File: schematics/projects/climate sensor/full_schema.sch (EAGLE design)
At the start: 35 parts, among them Q1 KT3102BM, Q2 KT3102BM, Q3 KT3102BM, Q4 KT3102BM, Q5 KT3102BM

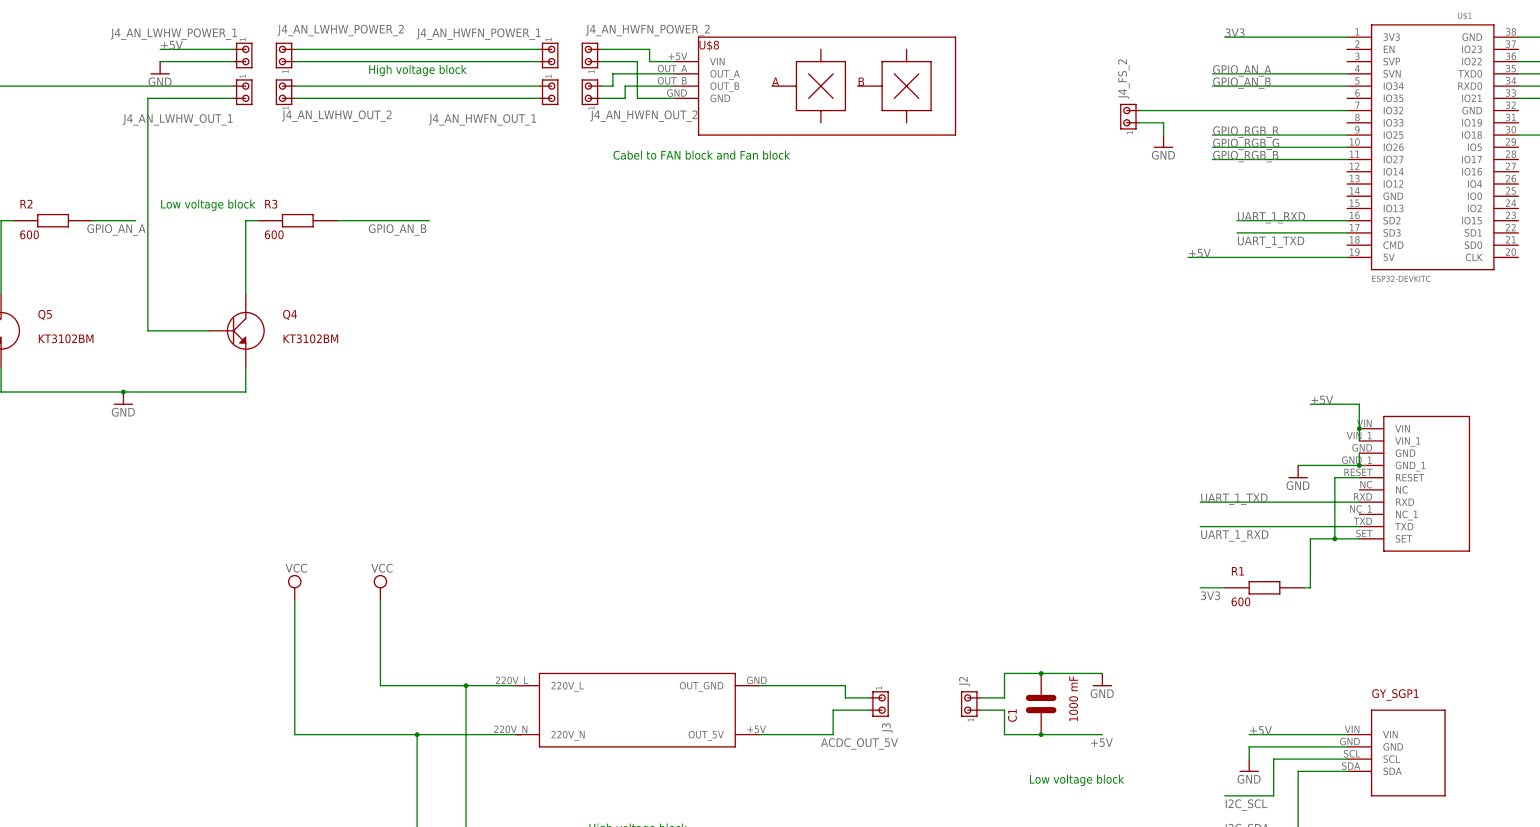
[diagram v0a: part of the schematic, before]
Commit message: added eagle board files for low-voltage schemas
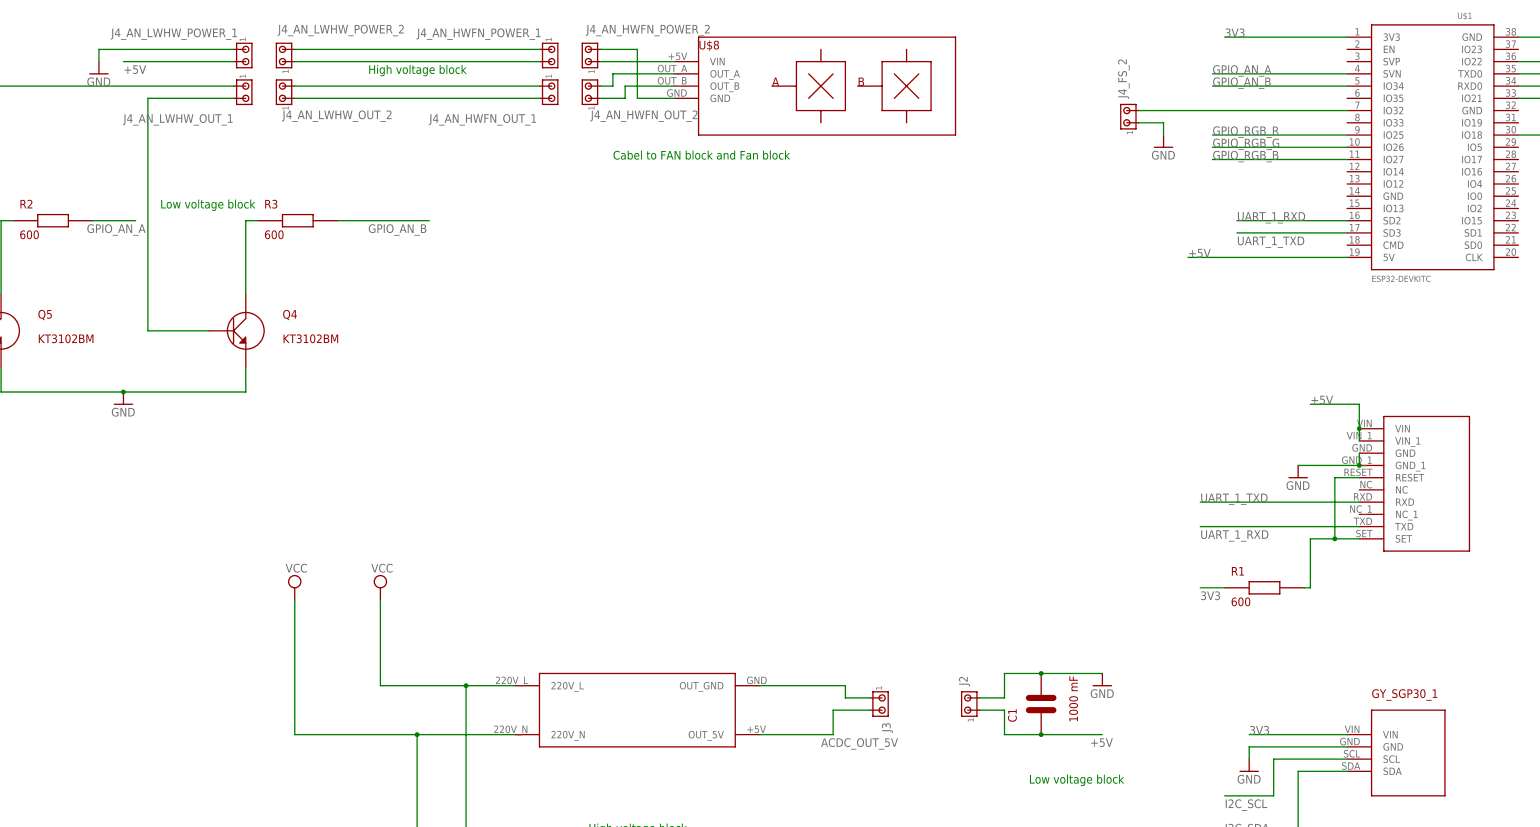
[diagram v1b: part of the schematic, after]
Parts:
- renumbered GY_SGP1 to GY_SGP30_1
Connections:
- net +5V: now also J4_AN_LWHW_POWER_1.2; no longer GY_SGP30_1.VIN, J4_AN_LWHW_POWER_1.1
- net 3V3: now also GY_SGP30_1.VIN
- net GND: now also J4_AN_HWFN_POWER_2.2, J4_AN_LWHW_POWER_1.1; no longer J4_AN_HWFN_POWER_2.1, J4_AN_LWHW_POWER_1.2
- net N$12: now also J4_AN_HWFN_POWER_2.1; no longer J4_AN_HWFN_POWER_2.2
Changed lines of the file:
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@@
 <part name="U$10" library="my_devices" deviceset="FAN" device=""/>
 <part name="U$3" library="my_devices" deviceset="PMS7003" device=""/>
-<part name="GY_SGP1" library="my_devices" deviceset="GY-SGP30" device=""/>
+<part name="GY_SGP30_1" library="my_devices" deviceset="GY-SGP30" device=""/>
 <part name="U$5" library="my_devices" deviceset="TTP223" device=""/>
 <part name="U$6" library="my_devices" deviceset="RGBLED" device=""/>
@@
 <part name="J4_AN_HWFN_POWER_2" library="con-amp" library_urn="urn:adsk.eagle:library:127" deviceset="MTA02-100" device="" package3d_urn="urn:adsk.eagle:package:8081649/1"/>
 <part name="J4_AN_HWFN_OUT_2" library="con-amp" library_urn="urn:adsk.eagle:library:127" deviceset="MTA02-100" device="" package3d_urn="urn:adsk.eagle:package:8081649/1"/>
-<part name="GND10" library="supply1" library_urn="urn:adsk.eagle:library:371" deviceset="GND" device=""/>
 <part name="J8" library="con-amp" library_urn="urn:adsk.eagle:library:127" deviceset="MTA02-100" device="" package3d_urn="urn:adsk.eagle:package:8081649/1"/>
 <part name="J9" library="con-amp" library_urn="urn:adsk.eagle:library:127" deviceset="MTA02-100" device="" package3d_urn="urn:adsk.eagle:package:8081649/1"/>
@@
 <part name="J4_AN_HWFN_OUT_1" library="con-amp" library_urn="urn:adsk.eagle:library:127" deviceset="MTA02-100" device="" package3d_urn="urn:adsk.eagle:package:8081649/1"/>
 <part name="J4_AN_HWFN_POWER_1" library="con-amp" library_urn="urn:adsk.eagle:library:127" deviceset="MTA02-100" device="" package3d_urn="urn:adsk.eagle:package:8081649/1"/>
+<part name="GND3" library="supply1" library_urn="urn:adsk.eagle:library:371" deviceset="GND" device=""/>
 </parts>
 <sheets>
@@
 <instance part="U$10" gate="G$1" x="-93.98" y="-106.68" smashed="yes" rot="R90" grouprefs="FAN"/>
 <instance part="U$3" gate="G$1" x="-38.1" y="10.16" smashed="yes" grouprefs="PMS7003"/>
-<instance part="GY_SGP1" gate="G$1" x="-48.26" y="-43.18" smashed="yes" grouprefs="GY-SGP30">
+<instance part="GY_SGP30_1" gate="G$1" x="-48.26" y="-43.18" smashed="yes" grouprefs="GY-SGP30">
 <attribute name="NAME" x="-50.8" y="-33.02" size="1.778" layer="94"/>
 </instance>
@@
 <attribute name="VALUE" x="-209.55" y="96.52" size="1.778" layer="96" rot="R90"/>
 </instance>
-<instance part="GND10" gate="1" x="-302.26" y="96.52" smashed="yes" grouprefs="ANEMOMETER">
-<attribute name="VALUE" x="-304.8" y="93.98" size="1.778" layer="96"/>
-</instance>
 <instance part="J8" gate="G$1" x="-149.86" y="-109.22" smashed="yes" rot="R270" grouprefs="FAN_SWITCH">
 <attribute name="NAME" x="-149.86" y="-114.3" size="1.778" layer="95" rot="R270"/>
@@
 <attribute name="NAME" x="-248.92" y="104.14" size="1.778" layer="95"/>
 <attribute name="VALUE" x="-224.79" y="96.52" size="1.778" layer="96" rot="R270"/>
+</instance>
+<instance part="GND3" gate="1" x="-314.96" y="96.52" smashed="yes" grouprefs="ANEMOMETER">
+<attribute name="VALUE" x="-317.5" y="93.98" size="1.778" layer="96"/>
 </instance>
 </instances>
@@
 <pinref part="GND6" gate="1" pin="GND"/>
 <wire x1="-76.2" y1="-43.18" x2="-76.2" y2="-45.72" width="0.1524" layer="91" grouprefs="GY-SGP30"/>
-<pinref part="GY_SGP1" gate="G$1" pin="GND"/>
+<pinref part="GY_SGP30_1" gate="G$1" pin="GND"/>
 </segment>
 <segment>
@@
 </segment>
 <segment>
-<pinref part="GND10" gate="1" pin="GND"/>
-<pinref part="J4_AN_LWHW_POWER_1" gate="G$1" pin="2"/>
-<wire x1="-302.26" y1="99.06" x2="-287.02" y2="99.06" width="0.1524" layer="91" grouprefs="ANEMOMETER"/>
-</segment>
-<segment>
 <pinref part="J2" gate="G$1" pin="2"/>
 <wire x1="-132.08" y1="-33.02" x2="-127" y2="-33.02" width="0.1524" layer="91" grouprefs="5V_SUPPLY_JET"/>
@@
 </segment>
 <segment>
+<pinref part="J4_AN_LWHW_POWER_1" gate="G$1" pin="1"/>
+<wire x1="-287.02" y1="101.6" x2="-314.96" y2="101.6" width="0.1524" layer="91" grouprefs="ANEMOMETER"/>
+<wire x1="-314.96" y1="101.6" x2="-314.96" y2="99.06" width="0.1524" layer="91" grouprefs="ANEMOMETER"/>
+<pinref part="GND3" gate="1" pin="GND"/>
+</segment>
+<segment>
+<pinref part="J4_AN_HWFN_POWER_2" gate="G$1" pin="2"/>
+<wire x1="-210.82" y1="101.6" x2="-203.2" y2="101.6" width="0.1524" layer="91" grouprefs="ANEMOMETER"/>
+<wire x1="-203.2" y1="101.6" x2="-203.2" y2="91.44" width="0.1524" layer="91" grouprefs="ANEMOMETER"/>
 <pinref part="U$8" gate="G$1" pin="GND"/>
-<wire x1="-195.58" y1="91.44" x2="-203.2" y2="91.44" width="0.1524" layer="91" grouprefs="ANEMOMETER"/>
-<wire x1="-203.2" y1="91.44" x2="-203.2" y2="99.06" width="0.1524" layer="91" grouprefs="ANEMOMETER"/>
-<pinref part="J4_AN_HWFN_POWER_2" gate="G$1" pin="1"/>
-<wire x1="-203.2" y1="99.06" x2="-210.82" y2="99.06" width="0.1524" layer="91" grouprefs="ANEMOMETER"/>
+<wire x1="-203.2" y1="91.44" x2="-195.58" y2="91.44" width="0.1524" layer="91" grouprefs="ANEMOMETER"/>
 </segment>
 </net>
@@
 <wire x1="-71.12" y1="-53.34" x2="-81.28" y2="-53.34" width="0.1524" layer="91" grouprefs="GY-SGP30"/>
 <label x="-81.28" y="-55.88" size="1.778" layer="95" grouprefs="GY-SGP30"/>
-<pinref part="GY_SGP1" gate="G$1" pin="SCL"/>
+<pinref part="GY_SGP30_1" gate="G$1" pin="SCL"/>
 </segment>
 </net>
@@
 <wire x1="-66.04" y1="-60.96" x2="-81.28" y2="-60.96" width="0.1524" layer="91" grouprefs="GY-SGP30"/>
 <label x="-81.28" y="-60.96" size="1.778" layer="95" grouprefs="GY-SGP30"/>
-<pinref part="GY_SGP1" gate="G$1" pin="SDA"/>
+<pinref part="GY_SGP30_1" gate="G$1" pin="SDA"/>
 </segment>
 </net>
@@
 <wire x1="-88.9" y1="58.42" x2="-55.88" y2="58.42" width="0.1524" layer="91" grouprefs="ESP"/>
 <label x="-88.9" y="58.42" size="1.778" layer="95" grouprefs="ESP"/>
-</segment>
-<segment>
-<wire x1="-55.88" y1="-40.64" x2="-76.2" y2="-40.64" width="0.1524" layer="91" grouprefs="GY-SGP30"/>
-<label x="-76.2" y="-40.64" size="1.778" layer="95" grouprefs="GY-SGP30"/>
-<pinref part="GY_SGP1" gate="G$1" pin="VIN"/>
-</segment>
-<segment>
-<pinref part="J4_AN_LWHW_POWER_1" gate="G$1" pin="1"/>
-<wire x1="-287.02" y1="101.6" x2="-302.26" y2="101.6" width="0.1524" layer="91" grouprefs="ANEMOMETER"/>
-<label x="-302.26" y="101.6" size="1.778" layer="95" grouprefs="ANEMOMETER"/>
 </segment>
 <segment>
@@
 <wire x1="76.2" y1="33.02" x2="55.88" y2="33.02" width="0.1524" layer="91" grouprefs="MH_Z19B_CO2"/>
 <label x="53.34" y="33.02" size="1.778" layer="95" grouprefs="MH_Z19B_CO2"/>
+</segment>
+<segment>
+<pinref part="J4_AN_LWHW_POWER_1" gate="G$1" pin="2"/>
+<wire x1="-287.02" y1="99.06" x2="-309.88" y2="99.06" width="0.1524" layer="91" grouprefs="ANEMOMETER"/>
+<label x="-309.88" y="96.52" size="1.778" layer="95" grouprefs="ANEMOMETER"/>
 </segment>
 </net>
@@
 <label x="-86.36" y="-12.7" size="1.778" layer="95" grouprefs="PMS7003"/>
 </segment>
+<segment>
+<wire x1="-55.88" y1="-40.64" x2="-76.2" y2="-40.64" width="0.1524" layer="91" grouprefs="GY-SGP30"/>
+<label x="-76.2" y="-40.64" size="1.778" layer="95" grouprefs="GY-SGP30"/>
+<pinref part="GY_SGP30_1" gate="G$1" pin="VIN"/>
+</segment>
 </net>
 <net name="UART_0_TXD" class="0">
@@
 </segment>
 </net>
-<net name="N$12" class="0">
-<segment>
-<pinref part="U$8" gate="G$1" pin="VIN"/>
-<wire x1="-195.58" y1="99.06" x2="-200.66" y2="99.06" width="0.1524" layer="91" grouprefs="ANEMOMETER"/>
-<wire x1="-200.66" y1="99.06" x2="-200.66" y2="101.6" width="0.1524" layer="91" grouprefs="ANEMOMETER"/>
-<pinref part="J4_AN_HWFN_POWER_2" gate="G$1" pin="2"/>
-<wire x1="-200.66" y1="101.6" x2="-210.82" y2="101.6" width="0.1524" layer="91" grouprefs="ANEMOMETER"/>
-</segment>
-</net>
 <net name="N$13" class="0">
 <segment>
@@
 </segment>
 </net>
+<net name="N$12" class="0">
+<segment>
+<pinref part="J4_AN_HWFN_POWER_2" gate="G$1" pin="1"/>
+<pinref part="U$8" gate="G$1" pin="VIN"/>
+<wire x1="-210.82" y1="99.06" x2="-195.58" y2="99.06" width="0.1524" layer="91" grouprefs="ANEMOMETER"/>
+</segment>
+</net>

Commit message: actualized schematics
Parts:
- added R10, R4, R5, R6, R7, R8, R9: 600, my_devices:R
- C1: value 1000 mF -> 1000 uF
- Q1, Q2, Q3: value KT3102BM -> 2N3906BU; device my_devices:TRANSISTOR_NPN -> my_devices:TRANSISTOR_PNP
- Q4, Q5: value KT3102BM -> 2N3904
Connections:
- new net N$21: Q3.B, R4.P$2
- new net N$22: Q1.B, R5.P$2
- new net N$23: Q2.B, R6.P$2
- net +5V: now also J4_AN_LWHW_POWER_1.1, Q1.E, Q2.E, Q3.E, R10.P$2, R9.P$2; no longer J4_AN_LWHW_POWER_1.2
- net 3V3: now also R7.P$2, R8.P$2; no longer Q1.C, Q2.C, Q3.C
- net GND: now also J4_AN_HWFN_POWER_2.1, J4_AN_LWHW_POWER_1.2; no longer J4_AN_HWFN_POWER_2.2, J4_AN_LWHW_POWER_1.1
- net GPIO_RGB_B: now also R4.P$1; no longer Q3.B
- net GPIO_RGB_G: now also R5.P$1; no longer Q2.B
- net GPIO_RGB_R: now also R6.P$1; no longer Q1.B
- net N$1: now also Q3.C; no longer Q3.E
- net N$12: now also J4_AN_HWFN_POWER_2.2; no longer J4_AN_HWFN_POWER_2.1
- net N$2: now also Q1.C; no longer Q2.E
- net N$3: now also Q2.C; no longer Q1.E
- net N$4: now also R10.P$1
- net N$5: now also R9.P$1
- net N$6: now also R7.P$1
- net N$7: now also R8.P$1
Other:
- moved on the sheet: J4_AN_HWFN_OUT_1, J4_AN_HWFN_OUT_2, J4_AN_HWFN_POWER_1, J4_AN_HWFN_POWER_2, J4_AN_LWHW_OUT_1, J4_AN_LWHW_OUT_2, J4_AN_LWHW_POWER_1, J4_AN_LWHW_POWER_2, Q1, Q2, Q3, Q4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
